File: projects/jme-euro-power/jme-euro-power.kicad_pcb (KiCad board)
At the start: 2 copper layers, 31 parts, among them J1 12V AC, J2 Eurorack 16 pin male power co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, U1 LM7812T, U2 LM7912

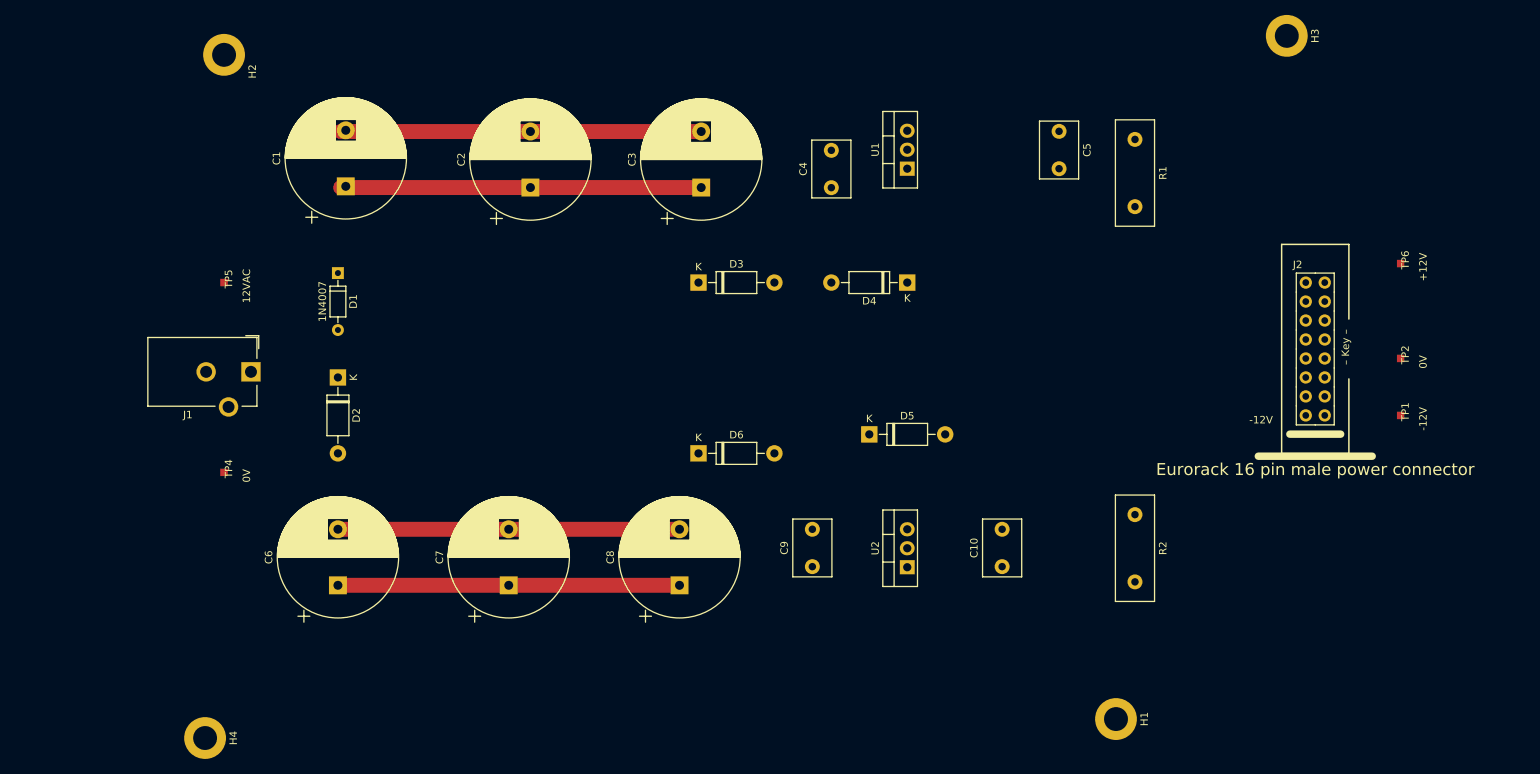
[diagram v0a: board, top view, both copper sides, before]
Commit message: Completed PCB optimized for stripboard. All warnings resolved.
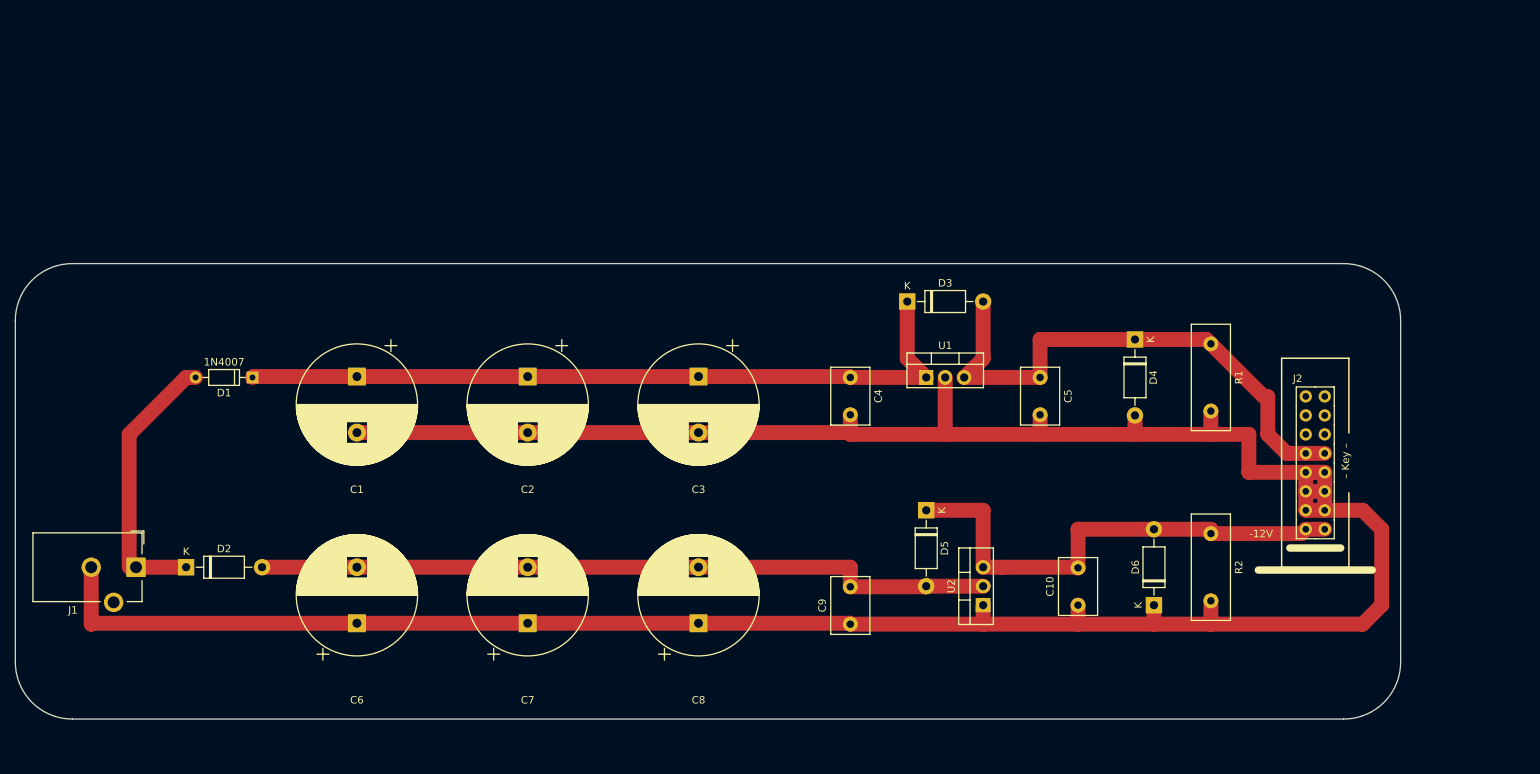
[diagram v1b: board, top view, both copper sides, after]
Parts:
- removed H1, H2, H3, H4: MountingHole_Pad, MountingHole:MountingHole_3.2mm_M3_DIN965_Pad
- removed TP1: -12V, 4ms_TestPoint:TestPoint_Pad_04
- removed TP2, TP4: 0V, 4ms_TestPoint:TestPoint_Pad_04
- removed TP5: 12VAC, 4ms_TestPoint:TestPoint_Pad_04
- removed TP6: +12V, 4ms_TestPoint:TestPoint_Pad_04
- moved D6 64.3 mm to (190.5, 134.6), turned to 90 degrees
- moved C5 33.0 mm to (175.3, 104.1)
- moved D2 32.5 mm to (61.0, 129.5), turned to 0 degrees
- moved D4 31.4 mm to (188.0, 99.1), turned to -90 degrees
- moved J1 30.3 mm to (54.3, 129.5)
- moved R1 29.2 mm to (198.1, 99.6)
- moved D3 28.1 mm to (157.5, 94.0)
- moved U1 28.1 mm to (160.0, 104.1), turned to 0 degrees
- moved C4 25.5 mm to (149.9, 104.1), turned to -90 degrees
- moved C1 25.5 mm to (83.8, 104.0), turned to -90 degrees
- moved C2 25.3 mm to (106.7, 104.0), turned to -90 degrees
- moved C3 25.3 mm to (129.5, 104.0), turned to -90 degrees
- moved D1 18.3 mm to (66.0, 104.1), turned to 180 degrees
- moved J2 15.2 mm to (212.1, 115.6)
- moved D5 12.7 mm to (160.0, 121.9), turned to -90 degrees
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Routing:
- net GND: track 94.0 -> 382.1 mm
- net +12V: track 0.00 -> 73.3 mm
- net -12V: track 0.00 -> 67.0 mm
- net Net-(D2-A): track 45.7 -> 99.2 mm
- net Net-(D1-K): track 48.3 -> 101.5 mm
- net Net-(D1-A): track 0.00 -> 36.5 mm
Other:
- board outline added: 185.4 x 61 mm

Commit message: Make layout smaller to accomodate strip board available.
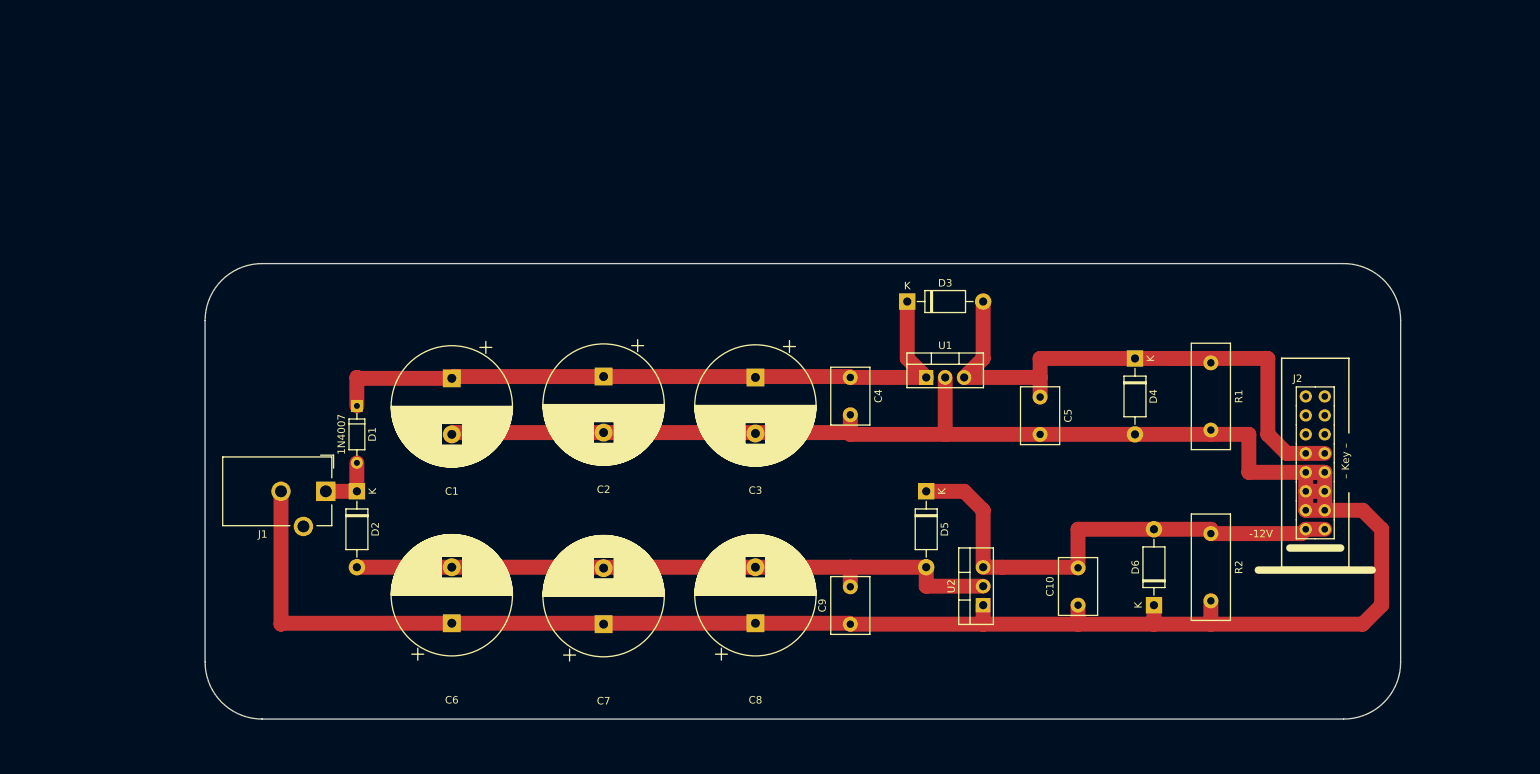
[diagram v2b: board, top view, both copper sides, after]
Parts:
- moved J1 27.4 mm to (79.7, 119.4)
- moved D2 25.0 mm to (83.8, 119.4), turned to -90 degrees
- moved D1 19.3 mm to (83.8, 111.8), turned to -90 degrees
- moved C1 12.7 mm to (96.5, 104.3)
- moved C6 12.7 mm to (96.5, 137.0)
- moved C7 10.2 mm to (116.8, 137.2)
- moved C2 10.2 mm to (116.8, 104.0)
- moved C3 7.62 mm to (137.2, 104.1)
- moved C8 7.62 mm to (137.2, 137.0)
- moved C5 2.62 mm to (175.3, 106.8)
- moved D5 2.54 mm to (160.0, 119.4)
- moved R1 2.54 mm to (198.1, 102.2)
- moved D4 2.54 mm to (188.0, 101.6)
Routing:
- net GND: track 382.1 -> 346.0 mm
- net Net-(D1-A): track 36.5 -> 7.97 mm
- net Net-(D2-A): track 99.2 -> 89.0 mm
- net Net-(D1-K): track 101.5 -> 91.4 mm
- net +12V: track 73.3 -> 81.2 mm
- net -12V: track 67.0 -> 68.0 mm
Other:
- board size 185.4 x 61 mm -> 160 x 61 mm

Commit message: incrmental update to power supply schematic
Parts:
- moved D3 9.16 mm to (149.9, 99.1), turned to 90 degrees
- turned U1 to 90 degrees
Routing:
- net +12V: track 81.2 -> 103.0 mm
- net GND: track 346.0 -> 356.1 mm
- net Net-(D1-K): track 91.4 -> 85.3 mm
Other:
- board size 160 x 61 mm -> 160 x 63.5 mm
